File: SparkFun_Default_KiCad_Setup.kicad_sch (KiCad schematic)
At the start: 12 parts

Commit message: Update fiducial symbol
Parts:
- removed FID1, FID2, FID3, FID4: Fiducial_0.5, SparkFun-Aesthetic:Fiducial_0.5mm_Mask1mm, symbol SparkFun-Aesthetic:Fiducial_0.5
- added FID1, FID2, FID3, FID4: Fiducial_0.5mm, SparkFun-Aesthetic:Fiducial_0.5mm_Mask1mm, symbol SparkFun-Aesthetic:Fiducial_0.5mm
- U1: renamed from U7; footprint SparkFun-Aesthetic:Ordering_Instructions -> SparkFun-Aesthetic:ORDERING_INSTRUCTIONS
- renumbered G5 to G1, G3 to G2, G1 to G3, ST3 to ST1, ST4 to ST2, ST1 to ST3, ST2 to ST4

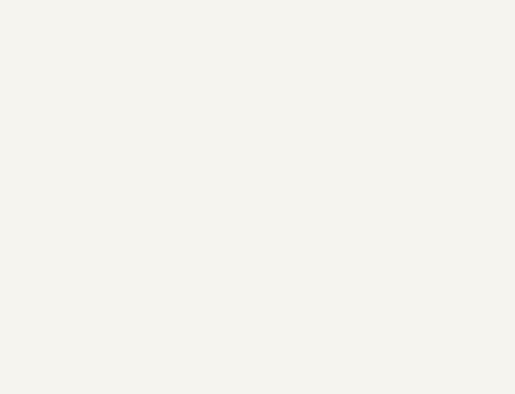
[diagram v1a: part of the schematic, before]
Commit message: Remove islands from polygon.
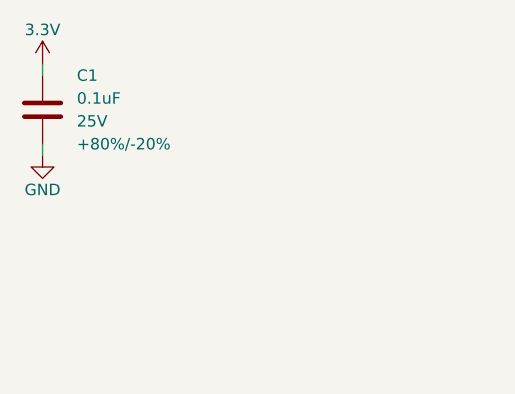
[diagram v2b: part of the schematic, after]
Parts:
- added C1: 0.1uF, SparkFun-Capacitor:C_0603_1608Metric, symbol SparkFun-Capacitor:0.1uF_0603_25V_20%
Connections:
- new net 3.3V: C1.1
- new net GND: C1.2
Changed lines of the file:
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@@
     (comment 1 "Designed by: ")
+  )
+  (wire (pts (xy 138.43 90.17) (xy 138.43 91.44))
+    (stroke (width 0) (type default))
+  )
+  (wire (pts (xy 138.43 100.33) (xy 138.43 99.06))
+    (stroke (width 0) (type default))
   )
   (symbol (lib_id "SparkFun-Hardware:Stand_off") (at 250.19 179.07 0) (unit 1)
@@
     )
   )
+  (symbol (lib_id "SparkFun-Capacitor:0.1uF_0603_25V_20%") (at 138.43 95.25 0) (unit 1)
+    (in_bom yes) (on_board yes) (dnp no) (fields_autoplaced)
+    (property "Reference" "C1" (at 142.24 91.44 0)
+      (effects (font (size 1.27 1.27)) (justify left))
+    )
+    (property "Value" "0.1uF" (at 142.24 93.98 0)
+      (effects (font (size 1.27 1.27)) (justify left))
+    )
+    (property "Footprint" "SparkFun-Capacitor:C_0603_1608Metric" (at 138.43 106.68 0)
+      (effects (font (size 1.27 1.27)) hide)
+    )
+    (property "Datasheet" "https://cdn.sparkfun.com/assets/8/a/4/a/5/Kemet_Capacitor_Datasheet.pdf" (at 138.43 109.22 0)
+      (effects (font (size 1.27 1.27)) hide)
+    )
+    (property "PROD_ID" "CAP-00810" (at 138.43 111.76 0)
+      (effects (font (size 1.27 1.27)) hide)
+    )
+    (property "Voltage" "25V" (at 142.24 96.52 0)
+      (effects (font (size 1.27 1.27)) (justify left))
+    )
+    (property "Tolerance" "+80%/-20%" (at 142.24 99.06 0)
+      (effects (font (size 1.27 1.27)) (justify left))
+    )
+    (pin "1")
+    (pin "2")
+    (instances
+      (project "SparkFun_Default_KiCad_Setup"
+        (path "/e3dd3ae4-244d-4cba-9cca-5d2abf83f29a"
+          (reference "C1") (unit 1)
+        )
+      )
+    )
+  )
   (symbol (lib_id "SparkFun-Aesthetic:Fiducial_0.5mm") (at 262.89 175.26 0) (unit 1)
     (in_bom yes) (on_board yes) (dnp no) (fields_autoplaced)
@@
         )
       )
+    )
+  )
+  (symbol (lib_id "SparkFun-PowerSymbol:3.3V") (at 138.43 90.17 0) (unit 1)
+    (in_bom yes) (on_board yes) (dnp no)
+    (property "Reference" "#PWR01" (at 138.43 93.98 0)
+      (effects (font (size 1.27 1.27)) hide)
+    )
+    (property "Value" "3.3V" (at 138.43 86.36 0)
+      (effects (font (size 1.27 1.27)))
+    )
+    (property "Footprint" "" (at 138.43 90.17 0)
+      (effects (font (size 1.27 1.27)) hide)
+    )
+    (property "Datasheet" "" (at 138.43 90.17 0)
+      (effects (font (size 1.27 1.27)) hide)
+    )
+    (pin "1")
+    (instances
+      (project "SparkFun_Default_KiCad_Setup"
+        (path "/e3dd3ae4-244d-4cba-9cca-5d2abf83f29a"
+          (reference "#PWR01") (unit 1)
+        )
+      )
+    )
+  )
+  (symbol (lib_id "SparkFun-PowerSymbol:GND") (at 138.43 100.33 0) (unit 1)
+    (in_bom yes) (on_board yes) (dnp no)
+    (property "Reference" "#PWR02" (at 138.43 106.68 0)
+      (effects (font (size 1.27 1.27)) hide)
+    )
+    (property "Value" "GND" (at 138.43 104.14 0)
+      (effects (font (size 1.27 1.27)))
+    )
+    (property "Footprint" "" (at 138.43 100.33 0)
+      (effects (font (size 1.27 1.27)) hide)
+    )
+    (property "Datasheet" "" (at 138.43 100.33 0)
+      (effects (font (size 1.27 1.27)) hide)
+    )
+    (pin "1")
+    (instances
+      (project "SparkFun_Default_KiCad_Setup"
+        (path "/e3dd3ae4-244d-4cba-9cca-5d2abf83f29a"
+          (reference "#PWR02") (unit 1)
+        )
+      )

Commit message: Update parts to new naming scheme
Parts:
- ST1, ST2, ST3, ST4: footprint SparkFun-Hardware:STAND-OFF -> SparkFun-Hardware:Standoff; symbol SparkFun-Hardware:Stand_off -> SparkFun-Hardware:Standoff
- U1: footprint SparkFun-Aesthetic:ORDERING_INSTRUCTIONS -> SparkFun-Aesthetic:Ordering_Instructions
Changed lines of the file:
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@@
     (stroke (width 0) (type default))
   )
-  (symbol (lib_id "SparkFun-Hardware:Stand_off") (at 250.19 179.07 0) (unit 1)
+  (symbol (lib_id "SparkFun-Hardware:Standoff") (at 250.19 179.07 0) (unit 1)
     (in_bom yes) (on_board yes) (dnp no)
     (property "Reference" "ST2" (at 250.19 176.53 0)
@@
       (effects (font (size 1.27 1.27)) hide)
     )
-    (property "Footprint" "SparkFun-Hardware:STAND-OFF" (at 250.19 184.15 0)
+    (property "Footprint" "SparkFun-Hardware:Standoff" (at 250.19 184.15 0)
       (effects (font (size 1.27 1.27)) hide)
     )
@@
       (effects (font (size 1.27 1.27)) hide)
     )
-    (property "Footprint" "SparkFun-Aesthetic:ORDERING_INSTRUCTIONS" (at 254 189.23 0)
+    (property "Footprint" "SparkFun-Aesthetic:Ordering_Instructions" (at 254 189.23 0)
       (effects (font (size 1.27 1.27)) hide)
     )
@@
     )
   )
-  (symbol (lib_id "SparkFun-Hardware:Stand_off") (at 254 179.07 0) (unit 1)
+  (symbol (lib_id "SparkFun-Hardware:Standoff") (at 254 179.07 0) (unit 1)
     (in_bom yes) (on_board yes) (dnp no)
     (property "Reference" "ST4" (at 254 176.53 0)
@@
       (effects (font (size 1.27 1.27)) hide)
     )
-    (property "Footprint" "SparkFun-Hardware:STAND-OFF" (at 254 184.15 0)
+    (property "Footprint" "SparkFun-Hardware:Standoff" (at 254 184.15 0)
       (effects (font (size 1.27 1.27)) hide)
     )
@@
     )
   )
-  (symbol (lib_id "SparkFun-Hardware:Stand_off") (at 250.19 175.26 0) (unit 1)
+  (symbol (lib_id "SparkFun-Hardware:Standoff") (at 250.19 175.26 0) (unit 1)
     (in_bom yes) (on_board yes) (dnp no)
     (property "Reference" "ST1" (at 250.19 172.72 0)
@@
       (effects (font (size 1.27 1.27)) hide)
     )
-    (property "Footprint" "SparkFun-Hardware:STAND-OFF" (at 250.19 180.34 0)
+    (property "Footprint" "SparkFun-Hardware:Standoff" (at 250.19 180.34 0)
       (effects (font (size 1.27 1.27)) hide)
     )
@@
     )
   )
-  (symbol (lib_id "SparkFun-Hardware:Stand_off") (at 254 175.26 0) (unit 1)
+  (symbol (lib_id "SparkFun-Hardware:Standoff") (at 254 175.26 0) (unit 1)
     (in_bom yes) (on_board yes) (dnp no) (fields_autoplaced)
     (property "Reference" "ST3" (at 254 172.72 0)
@@
       (effects (font (size 1.27 1.27)) hide)
     )
-    (property "Footprint" "SparkFun-Hardware:STAND-OFF" (at 254 180.34 0)
+    (property "Footprint" "SparkFun-Hardware:Standoff" (at 254 180.34 0)
       (effects (font (size 1.27 1.27)) hide)
     )

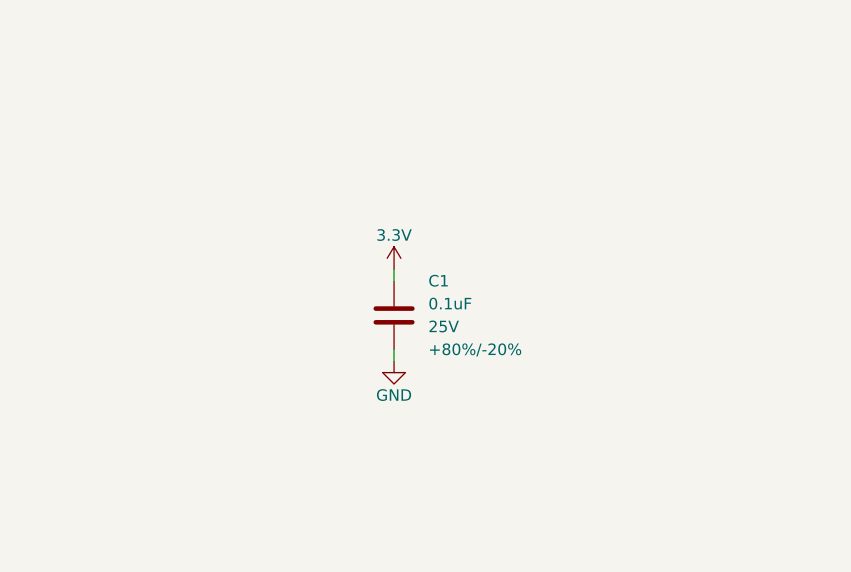
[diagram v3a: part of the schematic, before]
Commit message: Add basic regulator circuit to show various components
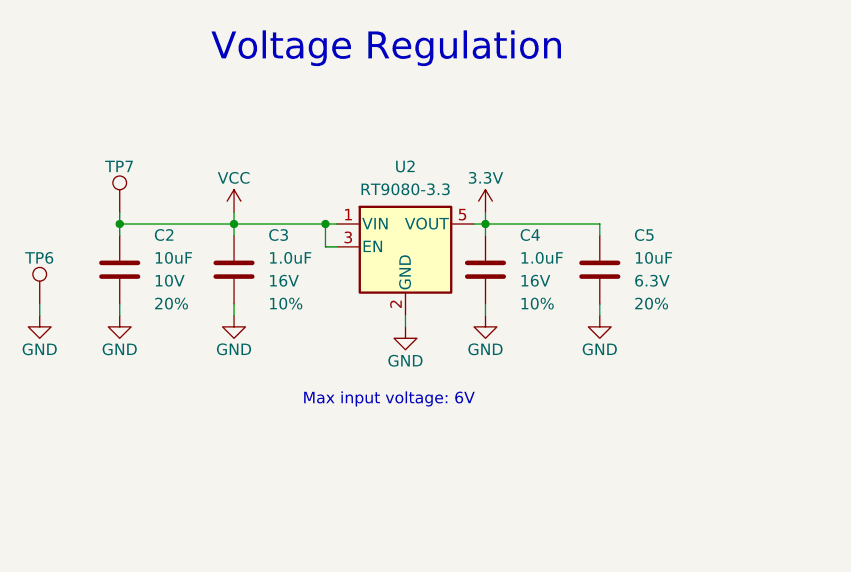
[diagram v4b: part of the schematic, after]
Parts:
- removed C1: 0.1uF, SparkFun-Capacitor:C_0603_1608Metric, symbol SparkFun-Capacitor:0.1uF_0603_25V_20%
- added C2: 10uF, SparkFun-Capacitor:C_0603_1608Metric, symbol SparkFun-Capacitor:10uF_0603_10V_20%
- added C3: 1.0uF, SparkFun-Capacitor:C_0603_1608Metric, symbol SparkFun-Capacitor:1.0uF_0603_16V_10%
- added C4: 1.0uF, SparkFun-Capacitor:C_0402_1005Metric, symbol SparkFun-Capacitor:1.0uF_0402_16V_10%
- added C5: 10uF, SparkFun-Capacitor:C_0603_1608Metric, symbol SparkFun-Capacitor:10uF_0603_6.3V_20%
- added TP6, TP7: TestPoint_0.75mm, SparkFun-Connector:TestPoint-0.75mm, symbol SparkFun-Connector:TestPoint_0.75mm
- added U2: RT9080-3.3, SparkFun-Semiconductor-Standard:SOT23-5, symbol SparkFun-Regulator:RT9080-3.3
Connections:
- net 3.3V: now also C4.1, C5.1, U2.5 (VOUT)
- net GND: now also C2.2, C3.2, C4.2, C5.2, TP6.1, U2.2 (GND)
- new net VCC: C2.1, C3.1, TP7.1, U2.1 (VIN), U2.3 (EN)
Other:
- note added: "Max input voltage: 6V"
- note added: "Voltage Regulation"

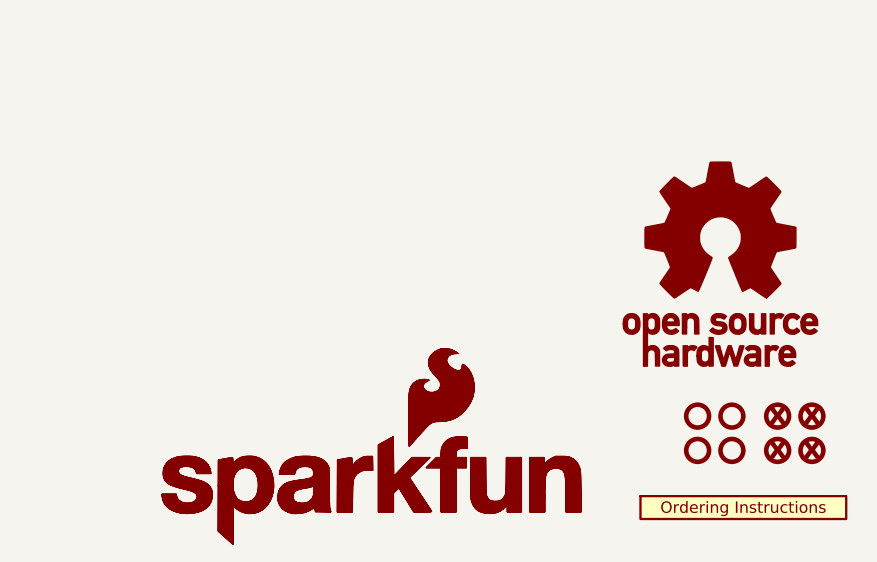
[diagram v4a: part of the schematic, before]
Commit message: Removing ordering instruction from SCH. Adding notes to PCB.
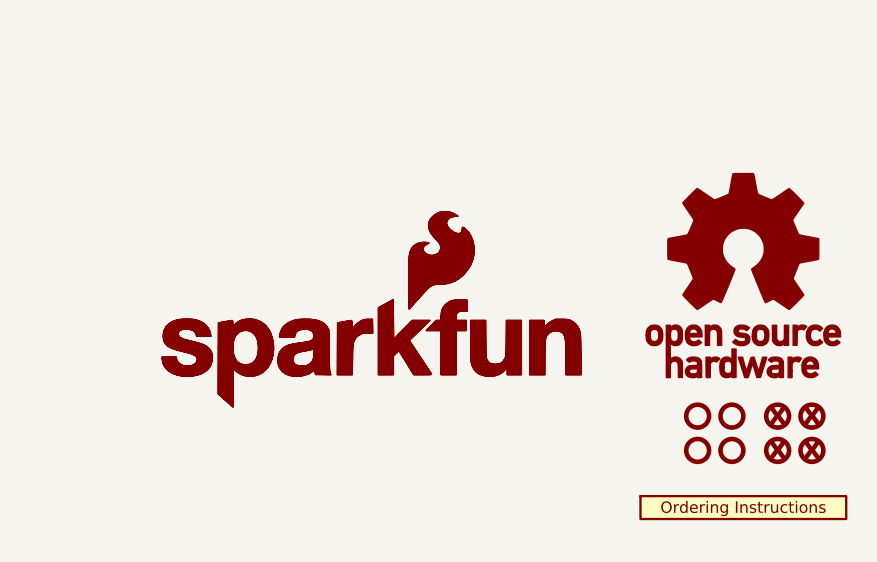
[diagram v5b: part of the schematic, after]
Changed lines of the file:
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@@
     )
   )
-  (symbol (lib_id "SparkFun-Aesthetic:SparkFun_Logo") (at 213.36 182.88 0) (unit 1)
+  (symbol (lib_id "SparkFun-Aesthetic:SparkFun_Logo") (at 213.36 167.64 0) (unit 1)
     (in_bom yes) (on_board no) (dnp no) (fields_autoplaced)
-    (property "Reference" "G1" (at 213.36 176.53 0)
-      (effects (font (size 1.27 1.27)) hide)
-    )
-    (property "Value" "SparkFun_Logo" (at 213.36 187.96 0)
-      (effects (font (size 1.27 1.27)) hide)
-    )
-    (property "Footprint" "SparkFun-Aesthetic:SparkFun_Logo_8mm" (at 213.36 190.5 0)
-      (effects (font (size 1.27 1.27)) hide)
-    )
-    (property "Datasheet" "" (at 217.173 179.0812 0)
+    (property "Reference" "G1" (at 213.36 161.29 0)
+      (effects (font (size 1.27 1.27)) hide)
+    )
+    (property "Value" "SparkFun_Logo" (at 213.36 172.72 0)
+      (effects (font (size 1.27 1.27)) hide)
+    )
+    (property "Footprint" "SparkFun-Aesthetic:SparkFun_Logo_8mm" (at 213.36 175.26 0)
+      (effects (font (size 1.27 1.27)) hide)
+    )
+    (property "Datasheet" "" (at 217.173 163.8412 0)
       (effects (font (size 1.27 1.27)) hide)
     )
@@
     )
   )
-  (symbol (lib_id "SparkFun-Aesthetic:OSHW_Logo") (at 252.73 162.56 0) (unit 1)
-    (in_bom no) (on_board yes) (dnp no) (fields_autoplaced)
-    (property "Reference" "G3" (at 252.73 146.05 0)
-      (effects (font (size 1.27 1.27)) hide)
-    )
-    (property "Value" "OSHW_Logo" (at 252.73 171.45 0)
-      (effects (font (size 1.27 1.27)) hide)
-    )
-    (property "Footprint" "SparkFun-Aesthetic:Creative_Commons_License" (at 252.9347 162.5843 0)
-      (effects (font (size 1.27 1.27)) hide)
-    )
-    (property "Datasheet" "" (at 252.9347 162.5843 0)
-      (effects (font (size 1.27 1.27)) hide)
-    )
-    (instances
-      (project "SparkFun_Default_KiCad_Setup"
-        (path "/e3dd3ae4-244d-4cba-9cca-5d2abf83f29a"
-          (reference "G3") (unit 1)
-        )
-      )
-    )
-  )
   (symbol (lib_id "SparkFun-Hardware:Standoff") (at 250.19 175.26 0) (unit 1)
     (in_bom yes) (on_board yes) (dnp no)
@@
     )
   )
+  (symbol (lib_id "SparkFun-Aesthetic:OSHW_Logo") (at 255.27 163.83 0) (unit 1)
+    (in_bom no) (on_board yes) (dnp no) (fields_autoplaced)
+    (property "Reference" "G3" (at 255.27 147.32 0)
+      (effects (font (size 1.27 1.27)) hide)
+    )
+    (property "Value" "OSHW_Logo" (at 255.27 172.72 0)
+      (effects (font (size 1.27 1.27)) hide)
+    )
+    (property "Footprint" "SparkFun-Aesthetic:Creative_Commons_License" (at 255.4747 163.8543 0)
+      (effects (font (size 1.27 1.27)) hide)
+    )
+    (property "Datasheet" "" (at 255.4747 163.8543 0)
+      (effects (font (size 1.27 1.27)) hide)
+    )
+    (instances
+      (project "SparkFun_Default_KiCad_Setup"
+        (path "/e3dd3ae4-244d-4cba-9cca-5d2abf83f29a"
+          (reference "G3") (unit 1)
+        )
+      )
+    )
+  )
   (symbol (lib_id "SparkFun-PowerSymbol:3.3V") (at 148.59 83.82 0) (unit 1)
     (in_bom yes) (on_board yes) (dnp no) (fields_autoplaced)
@@
     )
   )
-  (symbol (lib_id "SparkFun-Aesthetic:SparkFun_Logo") (at 213.36 182.88 0) (unit 1)
+  (symbol (lib_id "SparkFun-Aesthetic:SparkFun_Logo") (at 213.36 167.64 0) (unit 1)
     (in_bom yes) (on_board no) (dnp no) (fields_autoplaced)
-    (property "Reference" "G2" (at 213.36 176.53 0)
-      (effects (font (size 1.27 1.27)) hide)
-    )
-    (property "Value" "SparkFun_Logo" (at 213.36 187.96 0)
-      (effects (font (size 1.27 1.27)) hide)
-    )
-    (property "Footprint" "" (at 213.36 190.5 0)
-      (effects (font (size 1.27 1.27)) hide)
-    )
-    (property "Datasheet" "" (at 217.173 179.0812 0)
-      (effects (font (size 1.27 1.27)) hide)
-    )
+    (property "Reference" "G2" (at 213.36 161.29 0)
+      (effects (font (size 1.27 1.27)) hide)
+    )
+    (property "Value" "SparkFun_Logo" (at 213.36 172.72 0)
+      (effects (font (size 1.27 1.27)) hide)
+    )
+    (property "Footprint" "" (at 213.36 175.26 0)
+      (effects (font (size 1.27 1.27)) hide)
+    )
+    (property "Datasheet" "" (at 217.173 163.8412 0)
+      (effects (font (size 1.27 1.27)) hide)
+    )

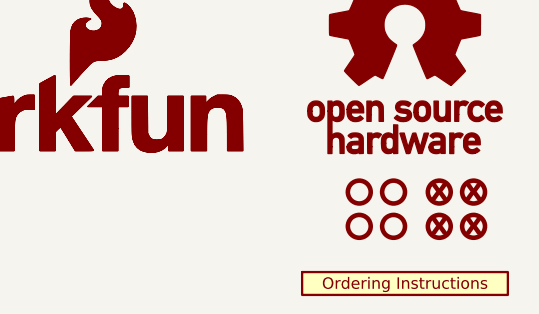
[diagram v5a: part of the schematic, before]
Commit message: Remove ordering instruction symbol from sch.
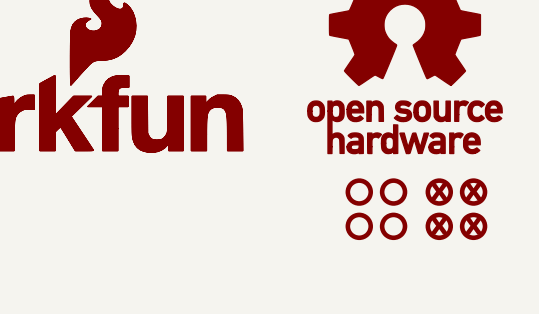
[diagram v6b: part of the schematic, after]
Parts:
- removed U1: ~, SparkFun-Aesthetic:Ordering_Instructions, symbol SparkFun-Aesthetic:Ordering_Instructions
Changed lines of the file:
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@@
-    )
-  )
-  (symbol (lib_id "SparkFun-Aesthetic:Ordering_Instructions") (at 254 185.42 0) (unit 1)
-    (in_bom yes) (on_board yes) (dnp no) (fields_autoplaced)
-    (property "Reference" "U1" (at 254 182.88 0)
-      (effects (font (size 1.27 1.27)) hide)
-    )
-    (property "Value" "~" (at 254 185.42 0)
-      (effects (font (size 1.27 1.27)) hide)
-    )
-    (property "Footprint" "SparkFun-Aesthetic:Ordering_Instructions" (at 254 189.23 0)
-      (effects (font (size 1.27 1.27)) hide)
-    )
-    (property "Datasheet" "" (at 254 185.42 0)
-      (effects (font (size 1.27 1.27)) hide)
-    )
-    (instances
-      (project "SparkFun_Default_KiCad_Setup"
-        (path "/e3dd3ae4-244d-4cba-9cca-5d2abf83f29a"
-          (reference "U1") (unit 1)
-        )
-      )
     )
   )

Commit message: Add title box defaults.
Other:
- title: (none) -> SparkFun Product (Qwiic)
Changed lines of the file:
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@@
   (paper "USLetter")
   (title_block
-    (date "2023-07-28")
+    (title "SparkFun Product (Qwiic)")
+    (date "2024-03-06")
     (rev "v10")
-    (comment 1 "Designed by: ")
+    (comment 1 "Designed by: You")
   )
   (junction (at 120.65 85.09) (diameter 0) (color 0 0 0 0)
